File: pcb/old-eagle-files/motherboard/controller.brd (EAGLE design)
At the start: 73.7 x 76.2 mm, 94 parts, among them J1 SNG-2MM-HEADER-04-V, J10 SNG-100-HEADER-01-HDR-V, J11 SNG-100-HEADER-01-HDR-V, J2 DL-1.25MM-HEADER-20, J3 MICRO_SD, J5 7498011122R, J6 USB_A, J7 DL-1.25MM-HEADER-10, J8 CUI-PJ-013C, J9 SNG-100-HEADER-01-HDR-V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

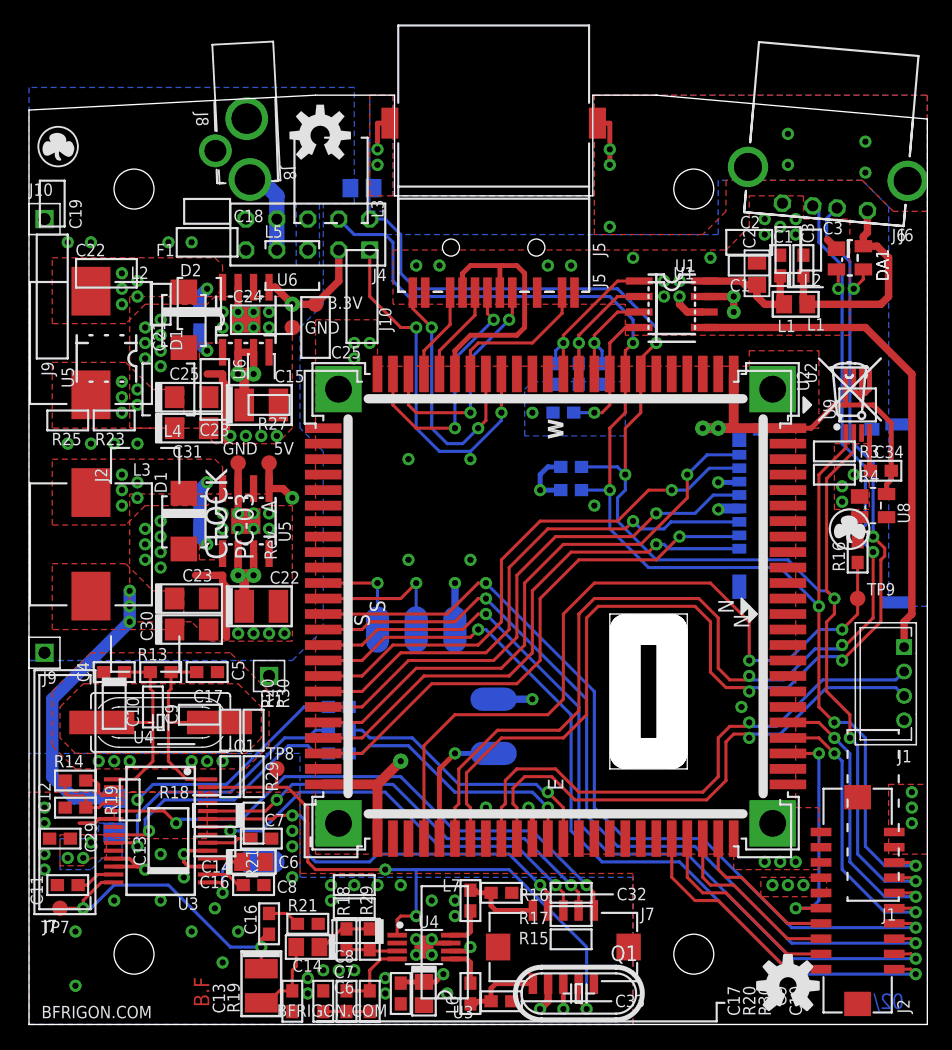
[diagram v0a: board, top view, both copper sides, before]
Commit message: Converted motherboard and left-panel project files to Kicad
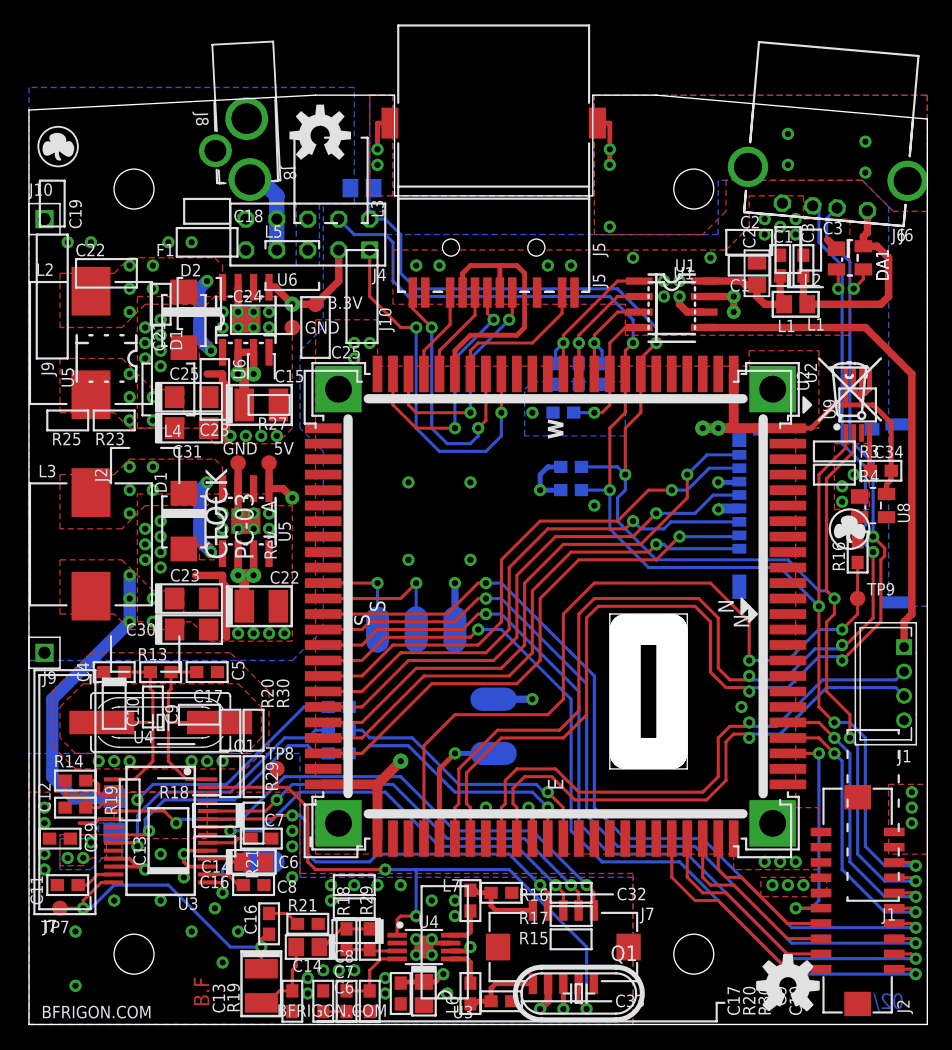
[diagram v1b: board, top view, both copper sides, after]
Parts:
- removed J11: SNG-100-HEADER-01-HDR-V, Connectors:HDR_M_1
- moved C24 0.64 mm to (14.0, 58.4)
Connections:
- removed net AD0: U2.W20
- removed net AD1: U2.W21
- removed net VREF: U2.W19
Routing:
- net 5V: track 156.4 -> 161.7 mm, vias 9 -> 11
- net 3.3V: track 121.8 -> 126.7 mm
- net BST_5V: track 1.95 -> 2.72 mm
- net BST_3.3V: track 1.95 -> 2.72 mm
- net V_AUX_ON: track 29.6 -> 30.3 mm
- net SPI_CS0: track 68.8 -> 69.6 mm
- net SPCK: track 68.8 -> 69.6 mm
- net MOSI: track 68.8 -> 69.6 mm
- net MISO: track 68.8 -> 69.6 mm
- net GND: vias 127 -> 123
